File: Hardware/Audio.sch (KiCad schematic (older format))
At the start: 0 parts

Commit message: Getting down structure, some components created.
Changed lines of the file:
@@
 $Descr A4 11693 8268
 encoding utf-8
-Sheet 8 8
+Sheet 2 8
 Title ""
 Date ""
@@
 F0 "Codec" 50
 F1 "Codec.sch" 50
+F2 "i2s_SCLK" I L 4450 2700 50
+F3 "i2s_LRCLK" I L 4450 2800 50
+F4 "i2s_DOUT" I L 4450 2900 50
+F5 "i2s_DIN" O L 4450 3000 50
+F6 "i2c1_SCL" I L 4450 3300 50
+F7 "i2c1_SDA" B L 4450 3400 50
+F8 "MCLK" I L 4450 3100 50
+F9 "LineOut_R" O R 5550 2950 50
+F10 "LineOut_L" O R 5550 3050 50
 $EndSheet
 $Sheet
@@
 F0 "Amplifier" 50
 F1 "Amplifier.sch" 50
+F2 "LineOut_R" I L 6100 2950 50
+F3 "LineOut_L" I L 6100 3050 50
+F4 "LOut_P" O R 7250 2950 50
+F5 "LOut_N" O R 7250 3150 50
+F6 "ROut_N" O R 7250 3550 50
+F7 "ROut_P" O R 7250 3750 50
 $EndSheet
+Text HLabel 9450 3100 2    50   Output ~ 0
+LOut_P
+Text HLabel 9450 3200 2    50   Output ~ 0
+LOut_N
+Text HLabel 9450 3300 2    50   Output ~ 0
+ROut_N
+Text HLabel 9450 3400 2    50   Output ~ 0
+ROut_P
 $EndSCHEMATC

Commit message: Adding some connectivity.
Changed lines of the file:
@@
 F2 "LineOut_R" I L 6100 2950 50
 F3 "LineOut_L" I L 6100 3050 50
-F4 "LOut_P" O R 7250 2950 50
+F4 "LOut_P" O R 7250 3050 50
 F5 "LOut_N" O R 7250 3150 50
-F6 "ROut_N" O R 7250 3550 50
-F7 "ROut_P" O R 7250 3750 50
+F6 "ROut_N" O R 7250 3250 50
+F7 "ROut_P" O R 7250 3350 50
 $EndSheet
-Text HLabel 9450 3100 2    50   Output ~ 0
+Text HLabel 7400 3050 2    50   Output ~ 0
 LOut_P
-Text HLabel 9450 3200 2    50   Output ~ 0
+Text HLabel 7400 3150 2    50   Output ~ 0
 LOut_N
-Text HLabel 9450 3300 2    50   Output ~ 0
+Text HLabel 7400 3250 2    50   Output ~ 0
 ROut_N
-Text HLabel 9450 3400 2    50   Output ~ 0
+Text HLabel 7400 3350 2    50   Output ~ 0
 ROut_P
+Text HLabel 3950 2700 0    50   Input ~ 0
+i2s_SCLK
+Text HLabel 3950 2800 0    50   Input ~ 0
+i2s_LRCLK
+Text HLabel 3950 2900 0    50   Input ~ 0
+i2s_DOUT
+Text HLabel 3950 3100 0    50   Input ~ 0
+MCLK
+Text HLabel 3950 3300 0    50   Input ~ 0
+i2c1_SCL
+Text HLabel 3950 3400 0    50   Input ~ 0
+i2c1_SDA
+Text HLabel 3950 3000 0    50   Output ~ 0
+i2s_DIN
 $EndSCHEMATC

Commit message: Some passives to codec.
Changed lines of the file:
@@
 F3 "i2s_LRCLK" I L 4450 2800 50
 F4 "i2s_DOUT" I L 4450 2900 50
-F5 "i2s_DIN" O L 4450 3000 50
+F5 "i2s_DIN" O R 5550 4050 50
 F6 "i2c1_SCL" I L 4450 3300 50
 F7 "i2c1_SDA" B L 4450 3400 50
@@
 Text HLabel 3950 3400 0    50   Input ~ 0
 i2c1_SDA
-Text HLabel 3950 3000 0    50   Output ~ 0
+Text HLabel 5650 4050 2    50   Output ~ 0
 i2s_DIN
 $EndSCHEMATC

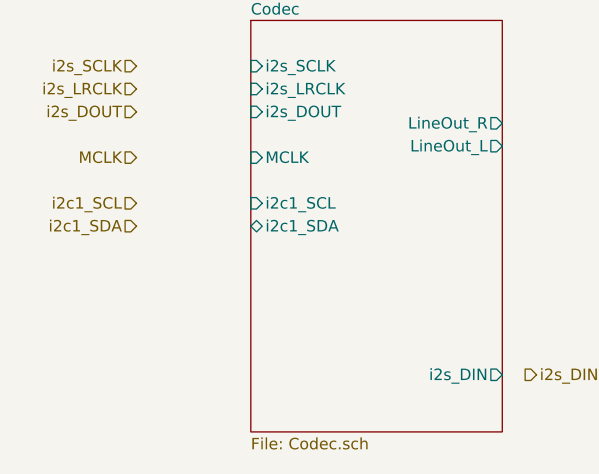
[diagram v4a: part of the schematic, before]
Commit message: More passives.
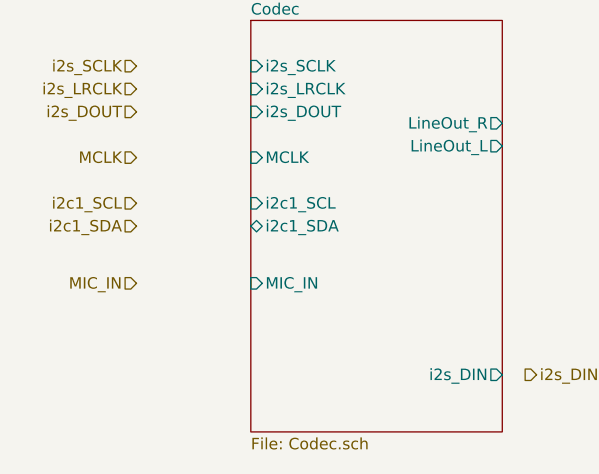
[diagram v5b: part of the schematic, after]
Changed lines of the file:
@@
 F9 "LineOut_R" O R 5550 2950 50
 F10 "LineOut_L" O R 5550 3050 50
+F11 "MIC_IN" I L 4450 3650 50
 $EndSheet
 $Sheet
@@
 Text HLabel 5650 4050 2    50   Output ~ 0
 i2s_DIN
+Text HLabel 3950 3650 0    50   Input ~ 0
+MIC_IN
 $EndSCHEMATC

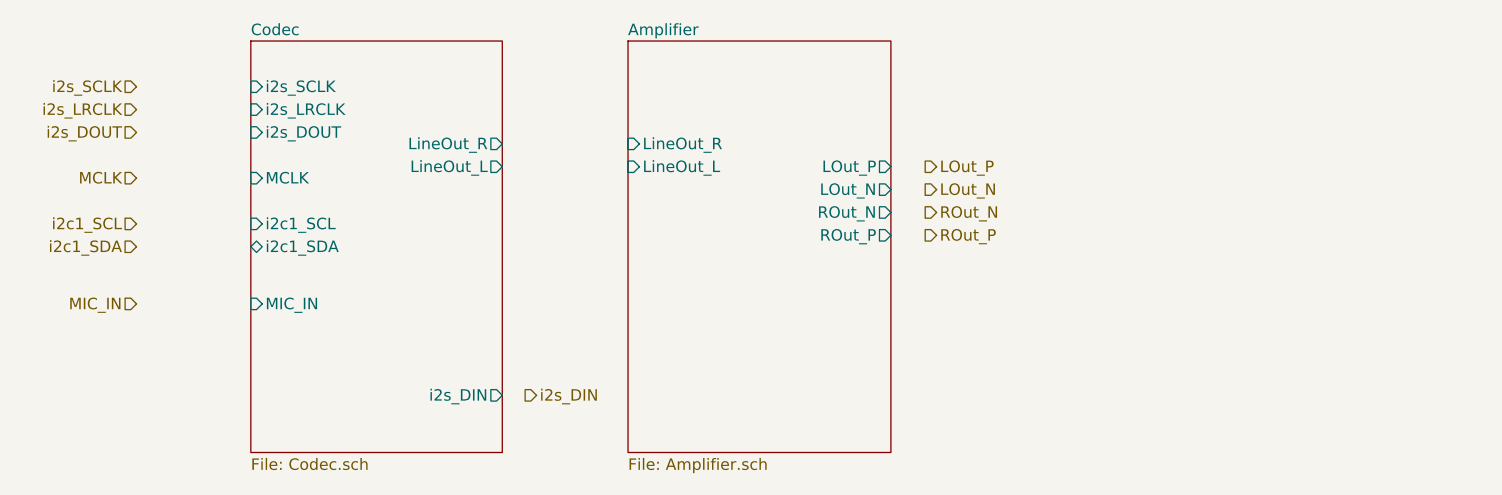
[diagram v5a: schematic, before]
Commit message: Adding in MEMS microphone library components.
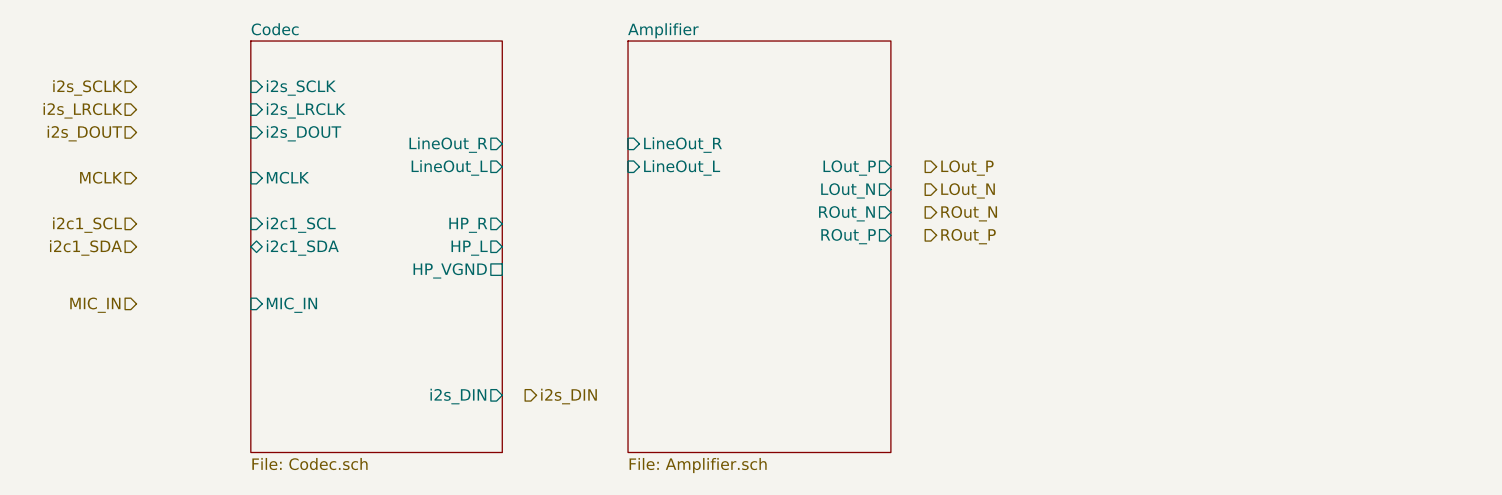
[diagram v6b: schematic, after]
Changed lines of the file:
@@
 F10 "LineOut_L" O R 5550 3050 50
 F11 "MIC_IN" I L 4450 3650 50
+F12 "HP_R" O R 5550 3300 50
+F13 "HP_L" O R 5550 3400 50
+F14 "HP_VGND" U R 5550 3500 50
 $EndSheet
 $Sheet

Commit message: Level shifting for DAC, some connectivity.
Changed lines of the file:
@@
 Text HLabel 3950 3650 0    50   Input ~ 0
 MIC_IN
+Text HLabel 5650 3300 2    50   Output ~ 0
+HP_R
+Text HLabel 5650 3400 2    50   Output ~ 0
+HP_L
+Text HLabel 5650 3500 2    50   UnSpc ~ 0
+HP_VGND
+Wire Wire Line
+	5550 3300 5650 3300
+Wire Wire Line
+	5550 3400 5650 3400
+Wire Wire Line
+	5550 3500 5650 3500
+Wire Wire Line
+	5550 4050 5650 4050
+Wire Wire Line
+	5550 3050 6100 3050
+Wire Wire Line
+	5550 2950 6100 2950
+Wire Wire Line
+	7250 3050 7400 3050
+Wire Wire Line
+	7250 3150 7400 3150
+Wire Wire Line
+	7250 3250 7400 3250
+Wire Wire Line
+	7250 3350 7400 3350
+Wire Wire Line
+	3950 2700 4450 2700
+Wire Wire Line
+	3950 2800 4450 2800
+Wire Wire Line
+	3950 2900 4450 2900
+Wire Wire Line
+	3950 3100 4450 3100
+Wire Wire Line
+	3950 3300 4450 3300
+Wire Wire Line
+	3950 3400 4450 3400
+Wire Wire Line
+	3950 3650 4450 3650
 $EndSCHEMATC

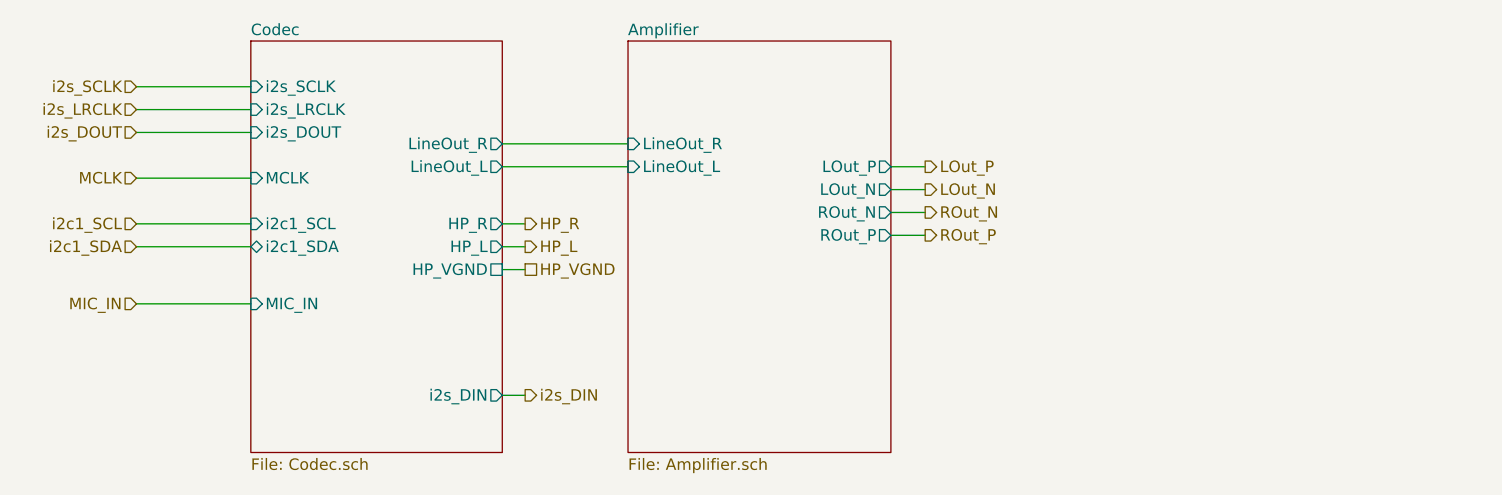
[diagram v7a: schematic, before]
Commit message: Hooking up switches, some more connectivity.
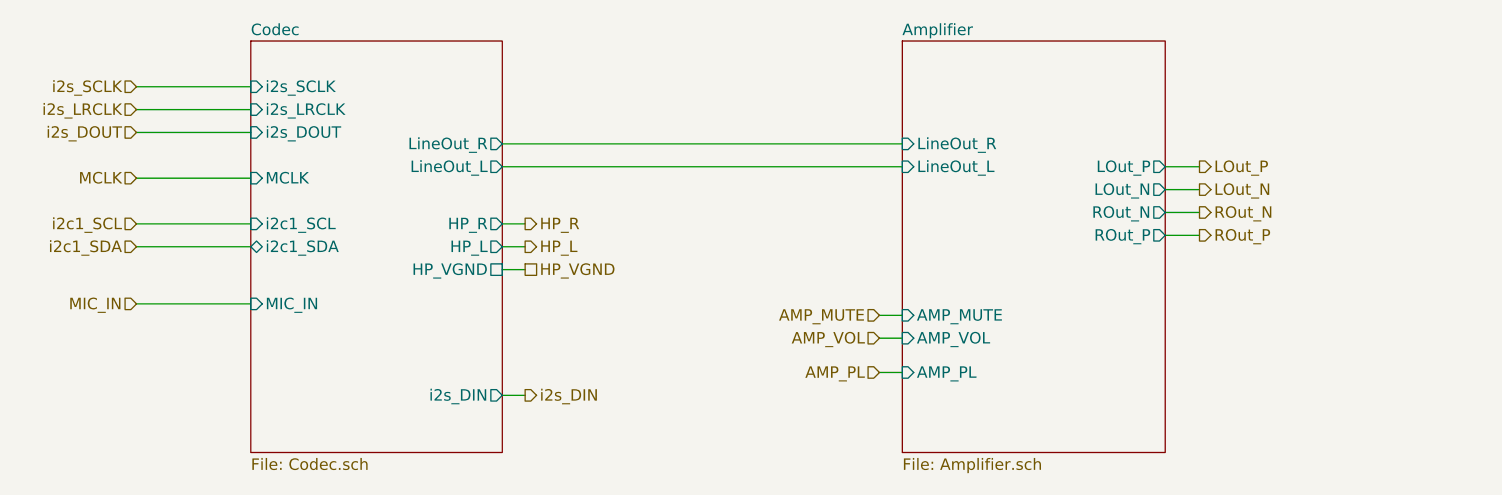
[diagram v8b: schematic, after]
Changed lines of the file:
@@
 $EndSheet
 $Sheet
-S 6100 2500 1150 1800
+S 7300 2500 1150 1800
 U 611E330D
 F0 "Amplifier" 50
 F1 "Amplifier.sch" 50
-F2 "LineOut_R" I L 6100 2950 50
-F3 "LineOut_L" I L 6100 3050 50
-F4 "LOut_P" O R 7250 3050 50
-F5 "LOut_N" O R 7250 3150 50
-F6 "ROut_N" O R 7250 3250 50
-F7 "ROut_P" O R 7250 3350 50
+F2 "LineOut_R" I L 7300 2950 50
+F3 "LineOut_L" I L 7300 3050 50
+F4 "LOut_P" O R 8450 3050 50
+F5 "LOut_N" O R 8450 3150 50
+F6 "ROut_N" O R 8450 3250 50
+F7 "ROut_P" O R 8450 3350 50
+F8 "AMP_VOL" I L 7300 3800 50
+F9 "AMP_PL" I L 7300 3950 50
+F10 "AMP_MUTE" I L 7300 3700 50
 $EndSheet
-Text HLabel 7400 3050 2    50   Output ~ 0
+Text HLabel 8600 3050 2    50   Output ~ 0
 LOut_P
-Text HLabel 7400 3150 2    50   Output ~ 0
+Text HLabel 8600 3150 2    50   Output ~ 0
 LOut_N
-Text HLabel 7400 3250 2    50   Output ~ 0
+Text HLabel 8600 3250 2    50   Output ~ 0
 ROut_N
-Text HLabel 7400 3350 2    50   Output ~ 0
+Text HLabel 8600 3350 2    50   Output ~ 0
 ROut_P
 Text HLabel 3950 2700 0    50   Input ~ 0
@@
 	5550 4050 5650 4050
 Wire Wire Line
-	5550 3050 6100 3050
+	5550 3050 7300 3050
 Wire Wire Line
-	5550 2950 6100 2950
+	5550 2950 7300 2950
 Wire Wire Line
-	7250 3050 7400 3050
+	8450 3050 8600 3050
 Wire Wire Line
-	7250 3150 7400 3150
+	8450 3150 8600 3150
 Wire Wire Line
-	7250 3250 7400 3250
+	8450 3250 8600 3250
 Wire Wire Line
-	7250 3350 7400 3350
+	8450 3350 8600 3350
 Wire Wire Line
 	3950 2700 4450 2700
@@
 Wire Wire Line
 	3950 3650 4450 3650
+Text HLabel 7200 3800 0    50   Input ~ 0
+AMP_VOL
+Wire Wire Line
+	7200 3800 7300 3800
+Text HLabel 7200 3950 0    50   Input ~ 0
+AMP_PL
+Wire Wire Line
+	7200 3950 7300 3950
+Text HLabel 7200 3700 0    50   Input ~ 0
+AMP_MUTE
+Wire Wire Line
+	7200 3700 7300 3700
 $EndSCHEMATC
